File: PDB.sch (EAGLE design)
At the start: 53 parts, among them J1 B06B-HCMKK, J2 B06B-HCMKK, J3 SS-6488-NF-A431, J4 SS-6488-NF-A431, J5 B06B-HCMKK, J6 B03B-HCMKS, J7 B03B-HCMKS, J8 SS-6488-NF-A431

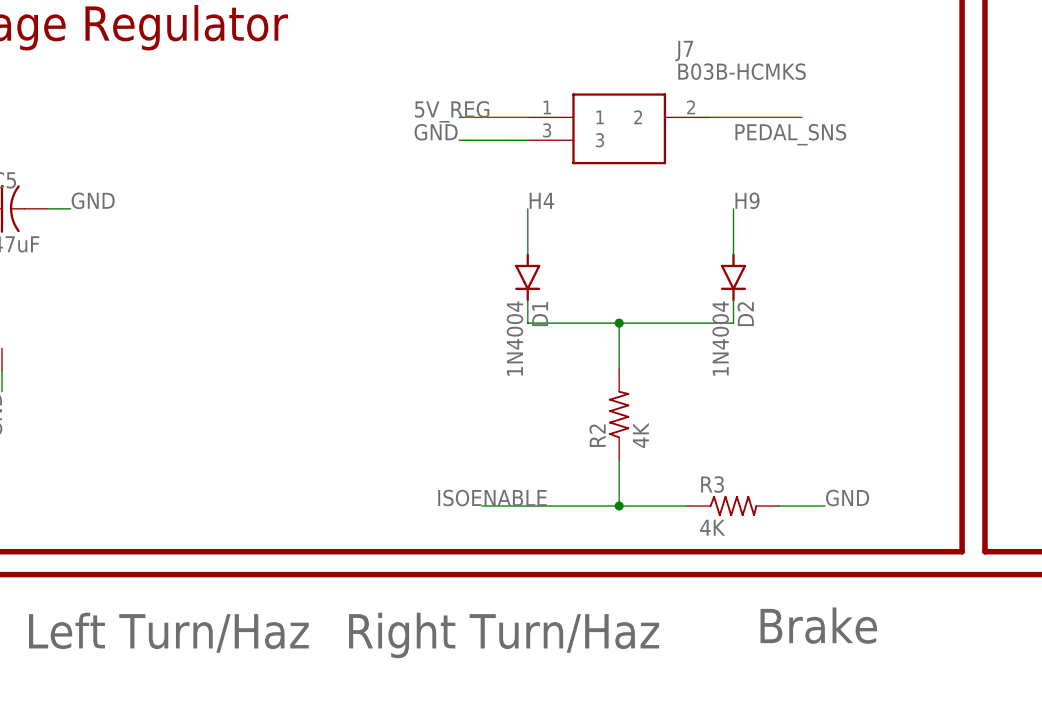
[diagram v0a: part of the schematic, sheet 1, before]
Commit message: Flipped all connectors to the back side, added capacitors connecting Teensy's 5V_REG to GND
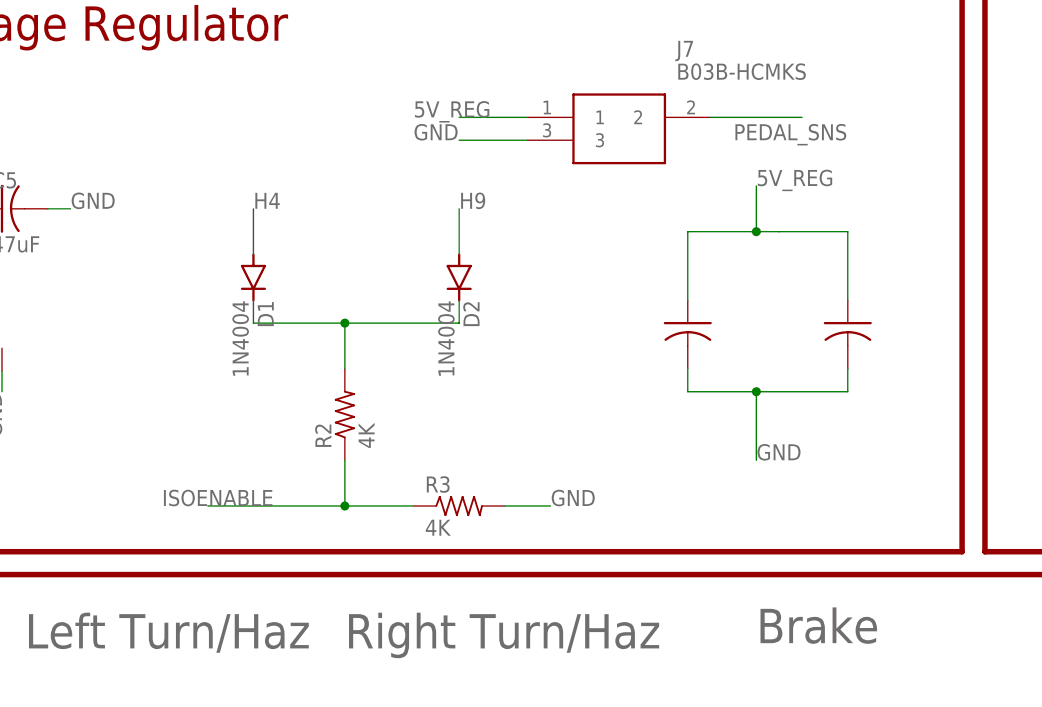
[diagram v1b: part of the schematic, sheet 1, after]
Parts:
- added C1: 0.1uF, rcl:C-USC0805
- added C2: 10uF, rcl:C-USC0805
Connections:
- net 5V_REG: now also C1.1, C2.1
- net GND: now also C1.2, C2.2
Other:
- moved on the sheet: D1, D2, R2, R3
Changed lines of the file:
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@@
 <part name="R2" library="master_library" deviceset="R-US_" device="R0805" package3d_urn="urn:adsk.eagle:package:2274104/1" value="4K"/>
 <part name="R3" library="master_library" deviceset="R-US_" device="R0805" package3d_urn="urn:adsk.eagle:package:2274104/1" value="4K"/>
+<part name="C1" library="rcl" library_urn="urn:adsk.eagle:library:334" deviceset="C-US" device="C0805" package3d_urn="urn:adsk.eagle:package:23617/2" value="0.1uF"/>
+<part name="C2" library="rcl" library_urn="urn:adsk.eagle:library:334" deviceset="C-US" device="C0805" package3d_urn="urn:adsk.eagle:package:23617/2" value="10uF"/>
 </parts>
 <sheets>
@@
 <attribute name="VALUE" x="223.012" y="119.888" size="1.778" layer="96" align="center-left"/>
 </instance>
-<instance part="D1" gate="1" x="-25.4" y="111.76" smashed="yes" rot="R270">
-<attribute name="NAME" x="-24.9174" y="109.22" size="1.778" layer="95" rot="R270"/>
-<attribute name="VALUE" x="-27.7114" y="109.22" size="1.778" layer="96" rot="R270"/>
-</instance>
-<instance part="D2" gate="1" x="-2.54" y="111.76" smashed="yes" rot="R270">
-<attribute name="NAME" x="-2.0574" y="109.22" size="1.778" layer="95" rot="R270"/>
-<attribute name="VALUE" x="-4.8514" y="109.22" size="1.778" layer="96" rot="R270"/>
-</instance>
-<instance part="R2" gate="G$1" x="-15.24" y="96.52" smashed="yes" rot="R90">
-<attribute name="NAME" x="-16.7386" y="92.71" size="1.778" layer="95" rot="R90"/>
-<attribute name="VALUE" x="-11.938" y="92.71" size="1.778" layer="96" rot="R90"/>
-</instance>
-<instance part="R3" gate="G$1" x="-2.54" y="86.36" smashed="yes">
-<attribute name="NAME" x="-6.35" y="87.8586" size="1.778" layer="95"/>
-<attribute name="VALUE" x="-6.35" y="83.058" size="1.778" layer="96"/>
-</instance>
+<instance part="D1" gate="1" x="-55.88" y="111.76" smashed="yes" rot="R270">
+<attribute name="NAME" x="-55.3974" y="109.22" size="1.778" layer="95" rot="R270"/>
+<attribute name="VALUE" x="-58.1914" y="109.22" size="1.778" layer="96" rot="R270"/>
+</instance>
+<instance part="D2" gate="1" x="-33.02" y="111.76" smashed="yes" rot="R270">
+<attribute name="NAME" x="-32.5374" y="109.22" size="1.778" layer="95" rot="R270"/>
+<attribute name="VALUE" x="-35.3314" y="109.22" size="1.778" layer="96" rot="R270"/>
+</instance>
+<instance part="R2" gate="G$1" x="-45.72" y="96.52" smashed="yes" rot="R90">
+<attribute name="NAME" x="-47.2186" y="92.71" size="1.778" layer="95" rot="R90"/>
+<attribute name="VALUE" x="-42.418" y="92.71" size="1.778" layer="96" rot="R90"/>
+</instance>
+<instance part="R3" gate="G$1" x="-33.02" y="86.36" smashed="yes">
+<attribute name="NAME" x="-36.83" y="87.8586" size="1.778" layer="95"/>
+<attribute name="VALUE" x="-36.83" y="83.058" size="1.778" layer="96"/>
+</instance>
+<instance part="C1" gate="G$1" x="10.16" y="106.68" smashed="yes"/>
+<instance part="C2" gate="G$1" x="-7.62" y="106.68" smashed="yes"/>
 </instances>
 <busses>
@@
 <segment>
 <pinref part="D1" gate="1" pin="A"/>
-<wire x1="-25.4" y1="114.3" x2="-25.4" y2="119.38" width="0.1524" layer="91"/>
-<label x="-25.4" y="119.38" size="1.778" layer="95"/>
+<wire x1="-55.88" y1="114.3" x2="-55.88" y2="119.38" width="0.1524" layer="91"/>
+<label x="-55.88" y="119.38" size="1.778" layer="95"/>
 </segment>
 </net>
@@
 <label x="-38.1" y="129.54" size="1.778" layer="95"/>
 </segment>
+<segment>
+<pinref part="C1" gate="G$1" pin="1"/>
+<wire x1="10.16" y1="109.22" x2="10.16" y2="116.84" width="0.1524" layer="91"/>
+<wire x1="10.16" y1="116.84" x2="2.54" y2="116.84" width="0.1524" layer="91"/>
+<pinref part="C2" gate="G$1" pin="1"/>
+<wire x1="0" y1="116.84" x2="-7.62" y2="116.84" width="0.1524" layer="91"/>
+<wire x1="-7.62" y1="109.22" x2="-7.62" y2="116.84" width="0.1524" layer="91"/>
+<wire x1="2.54" y1="116.84" x2="0" y2="116.84" width="0.1524" layer="91"/>
+<wire x1="0" y1="116.84" x2="0" y2="121.92" width="0.1524" layer="91"/>
+<junction x="0" y="116.84"/>
+<label x="0" y="121.92" size="1.778" layer="95"/>
+</segment>
 </net>
 <net name="10V_REG" class="0">
@@
 <segment>
 <pinref part="R3" gate="G$1" pin="2"/>
-<wire x1="2.54" y1="86.36" x2="7.62" y2="86.36" width="0.1524" layer="91"/>
-<label x="7.62" y="86.36" size="1.778" layer="95"/>
+<wire x1="-27.94" y1="86.36" x2="-22.86" y2="86.36" width="0.1524" layer="91"/>
+<label x="-22.86" y="86.36" size="1.778" layer="95"/>
+</segment>
+<segment>
+<pinref part="C1" gate="G$1" pin="2"/>
+<wire x1="10.16" y1="101.6" x2="10.16" y2="99.06" width="0.1524" layer="91"/>
+<wire x1="10.16" y1="99.06" x2="0" y2="99.06" width="0.1524" layer="91"/>
+<pinref part="C2" gate="G$1" pin="2"/>
+<wire x1="0" y1="99.06" x2="-7.62" y2="99.06" width="0.1524" layer="91"/>
+<wire x1="-7.62" y1="99.06" x2="-7.62" y2="101.6" width="0.1524" layer="91"/>
+<wire x1="0" y1="99.06" x2="0" y2="91.44" width="0.1524" layer="91"/>
+<junction x="0" y="99.06"/>
+<label x="0" y="91.44" size="1.778" layer="95"/>
 </segment>
 </net>
@@
 <segment>
 <pinref part="R2" gate="G$1" pin="1"/>
-<wire x1="-15.24" y1="91.44" x2="-15.24" y2="86.36" width="0.1524" layer="91"/>
-<wire x1="-15.24" y1="86.36" x2="-7.62" y2="86.36" width="0.1524" layer="91"/>
+<wire x1="-45.72" y1="91.44" x2="-45.72" y2="86.36" width="0.1524" layer="91"/>
+<wire x1="-45.72" y1="86.36" x2="-38.1" y2="86.36" width="0.1524" layer="91"/>
 <pinref part="R3" gate="G$1" pin="1"/>
-<wire x1="-15.24" y1="86.36" x2="-30.48" y2="86.36" width="0.1524" layer="91"/>
-<junction x="-15.24" y="86.36"/>
-<label x="-35.56" y="86.36" size="1.778" layer="95"/>
+<wire x1="-45.72" y1="86.36" x2="-60.96" y2="86.36" width="0.1524" layer="91"/>
+<junction x="-45.72" y="86.36"/>
+<label x="-66.04" y="86.36" size="1.778" layer="95"/>
 </segment>
 </net>
@@
 <segment>
 <pinref part="D2" gate="1" pin="A"/>
-<wire x1="-2.54" y1="114.3" x2="-2.54" y2="119.38" width="0.1524" layer="91"/>
-<label x="-2.54" y="119.38" size="1.778" layer="95"/>
+<wire x1="-33.02" y1="114.3" x2="-33.02" y2="119.38" width="0.1524" layer="91"/>
+<label x="-33.02" y="119.38" size="1.778" layer="95"/>
 </segment>
 </net>
@@
 <segment>
 <pinref part="D2" gate="1" pin="C"/>
-<wire x1="-2.54" y1="109.22" x2="-2.54" y2="106.68" width="0.1524" layer="91"/>
+<wire x1="-33.02" y1="109.22" x2="-33.02" y2="106.68" width="0.1524" layer="91"/>
 <pinref part="D1" gate="1" pin="C"/>
-<wire x1="-25.4" y1="109.22" x2="-25.4" y2="106.68" width="0.1524" layer="91"/>
-<wire x1="-2.54" y1="106.68" x2="-15.24" y2="106.68" width="0.1524" layer="91"/>
-<wire x1="-15.24" y1="106.68" x2="-25.4" y2="106.68" width="0.1524" layer="91"/>
-<wire x1="-15.24" y1="106.68" x2="-15.24" y2="101.6" width="0.1524" layer="91"/>
-<junction x="-15.24" y="106.68"/>
+<wire x1="-55.88" y1="109.22" x2="-55.88" y2="106.68" width="0.1524" layer="91"/>
+<wire x1="-33.02" y1="106.68" x2="-45.72" y2="106.68" width="0.1524" layer="91"/>
+<wire x1="-45.72" y1="106.68" x2="-55.88" y2="106.68" width="0.1524" layer="91"/>
+<wire x1="-45.72" y1="106.68" x2="-45.72" y2="101.6" width="0.1524" layer="91"/>
+<junction x="-45.72" y="106.68"/>
 <pinref part="R2" gate="G$1" pin="2"/>
 </segment>

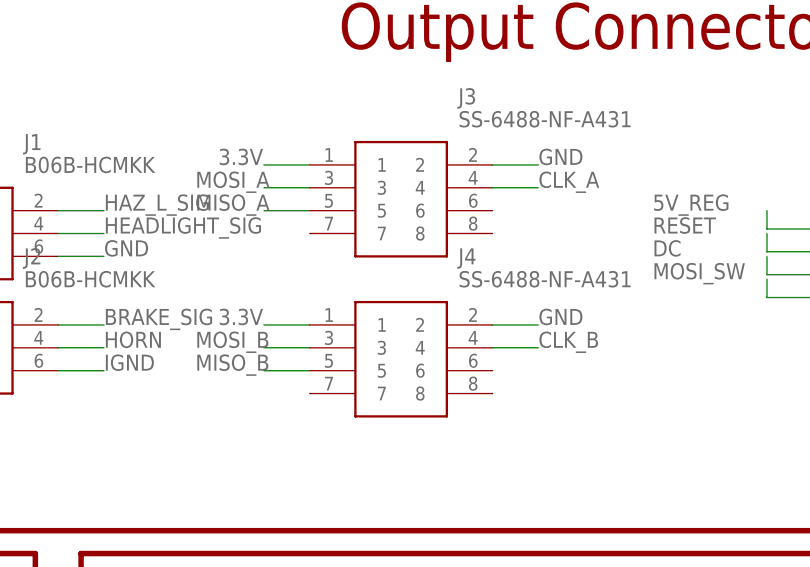
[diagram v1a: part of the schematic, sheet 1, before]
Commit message: Adjusted schematic and routing to pass twisted pairs to each signal
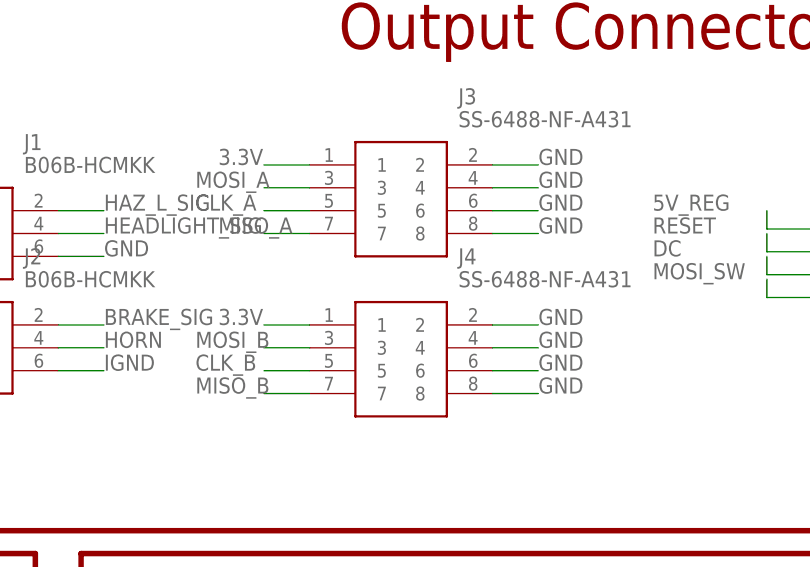
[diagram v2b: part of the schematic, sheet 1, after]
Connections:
- net CLK_A: now also J3.5; no longer J3.4
- net CLK_B: now also J4.5; no longer J4.4
- net GND: now also J3.4, J3.6, J3.8, J4.4, J4.6, J4.8
- net MISO_A: now also J3.7; no longer J3.5
- net MISO_B: now also J4.7; no longer J4.5
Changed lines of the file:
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@@
 <label x="0" y="91.44" size="1.778" layer="95"/>
+</segment>
+<segment>
+<pinref part="J3" gate="G$1" pin="4"/>
+<wire x1="170.18" y1="119.38" x2="175.26" y2="119.38" width="0.1524" layer="91"/>
+<label x="175.26" y="119.38" size="1.778" layer="95"/>
+</segment>
+<segment>
+<pinref part="J3" gate="G$1" pin="6"/>
+<wire x1="170.18" y1="116.84" x2="175.26" y2="116.84" width="0.1524" layer="91"/>
+<label x="175.26" y="116.84" size="1.778" layer="95"/>
+</segment>
+<segment>
+<pinref part="J3" gate="G$1" pin="8"/>
+<wire x1="170.18" y1="114.3" x2="175.26" y2="114.3" width="0.1524" layer="91"/>
+<label x="175.26" y="114.3" size="1.778" layer="95"/>
+</segment>
+<segment>
+<pinref part="J4" gate="G$1" pin="4"/>
+<wire x1="170.18" y1="101.6" x2="175.26" y2="101.6" width="0.1524" layer="91"/>
+<label x="175.26" y="101.6" size="1.778" layer="95"/>
+</segment>
+<segment>
+<pinref part="J4" gate="G$1" pin="6"/>
+<wire x1="170.18" y1="99.06" x2="175.26" y2="99.06" width="0.1524" layer="91"/>
+<label x="175.26" y="99.06" size="1.778" layer="95"/>
+</segment>
+<segment>
+<pinref part="J4" gate="G$1" pin="8"/>
+<wire x1="170.18" y1="96.52" x2="175.26" y2="96.52" width="0.1524" layer="91"/>
+<label x="175.26" y="96.52" size="1.778" layer="95"/>
 </segment>
 </net>
@@
 <net name="CLK_A" class="0">
 <segment>
-<pinref part="J3" gate="G$1" pin="4"/>
-<wire x1="170.18" y1="119.38" x2="175.26" y2="119.38" width="0.1524" layer="91"/>
-<label x="175.26" y="119.38" size="1.778" layer="95"/>
-</segment>
-<segment>
 <pinref part="U$3" gate="G$1" pin="D32/A13/SCK1/TX4"/>
 <wire x1="147.32" y1="-15.24" x2="142.24" y2="-15.24" width="0.1524" layer="91"/>
 <label x="139.7" y="-15.24" size="1.778" layer="95"/>
 </segment>
-</net>
-<net name="MISO_A" class="0">
 <segment>
 <pinref part="J3" gate="G$1" pin="5"/>
@@
 <label x="137.16" y="116.84" size="1.778" layer="95"/>
 </segment>
+</net>
+<net name="MISO_A" class="0">
 <segment>
 <pinref part="U$3" gate="G$1" pin="D1/TOUCH/MISO1/TX1"/>
@@
 <label x="134.62" y="43.18" size="1.778" layer="95"/>
 </segment>
+<segment>
+<pinref part="J3" gate="G$1" pin="7"/>
+<wire x1="149.86" y1="114.3" x2="144.78" y2="114.3" width="0.1524" layer="91"/>
+<label x="139.7" y="114.3" size="1.778" layer="95"/>
+</segment>
 </net>
 <net name="MOSI_B" class="0">
@@
 <net name="MISO_B" class="0">
 <segment>
+<pinref part="U$3" gate="G$1" pin="D12/MISO0"/>
+<wire x1="147.32" y1="15.24" x2="142.24" y2="15.24" width="0.1524" layer="91"/>
+<label x="137.16" y="15.24" size="1.778" layer="95"/>
+</segment>
+<segment>
+<pinref part="J4" gate="G$1" pin="7"/>
+<wire x1="149.86" y1="96.52" x2="144.78" y2="96.52" width="0.1524" layer="91"/>
+<label x="137.16" y="96.52" size="1.778" layer="95"/>
+</segment>
+</net>
+<net name="CLK_B" class="0">
+<segment>
+<pinref part="U$3" gate="G$1" pin="D13/LED/SCK0"/>
+<wire x1="218.44" y1="15.24" x2="226.06" y2="15.24" width="0.1524" layer="91"/>
+<label x="226.06" y="15.24" size="1.778" layer="95"/>
+</segment>
+<segment>
 <pinref part="J4" gate="G$1" pin="5"/>
 <wire x1="149.86" y1="99.06" x2="144.78" y2="99.06" width="0.1524" layer="91"/>
 <label x="137.16" y="99.06" size="1.778" layer="95"/>
 </segment>
-<segment>
-<pinref part="U$3" gate="G$1" pin="D12/MISO0"/>
-<wire x1="147.32" y1="15.24" x2="142.24" y2="15.24" width="0.1524" layer="91"/>
-<label x="137.16" y="15.24" size="1.778" layer="95"/>
-</segment>
-</net>
-<net name="CLK_B" class="0">
-<segment>
-<pinref part="J4" gate="G$1" pin="4"/>
-<wire x1="170.18" y1="101.6" x2="175.26" y2="101.6" width="0.1524" layer="91"/>
-<label x="175.26" y="101.6" size="1.778" layer="95"/>
-</segment>
-<segment>
-<pinref part="U$3" gate="G$1" pin="D13/LED/SCK0"/>
-<wire x1="218.44" y1="15.24" x2="226.06" y2="15.24" width="0.1524" layer="91"/>
-<label x="226.06" y="15.24" size="1.778" layer="95"/>
-</segment>
-</net>
+</net>

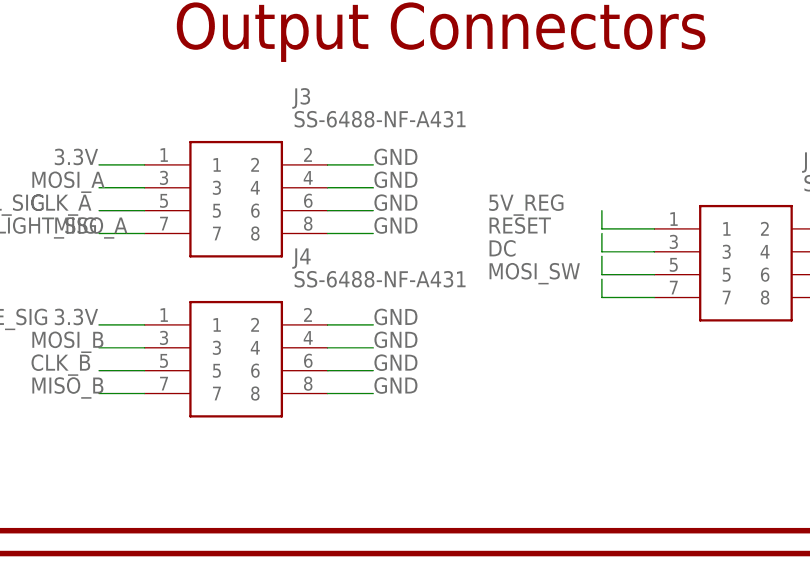
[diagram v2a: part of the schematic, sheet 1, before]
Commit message: adds cs signal but does not route it
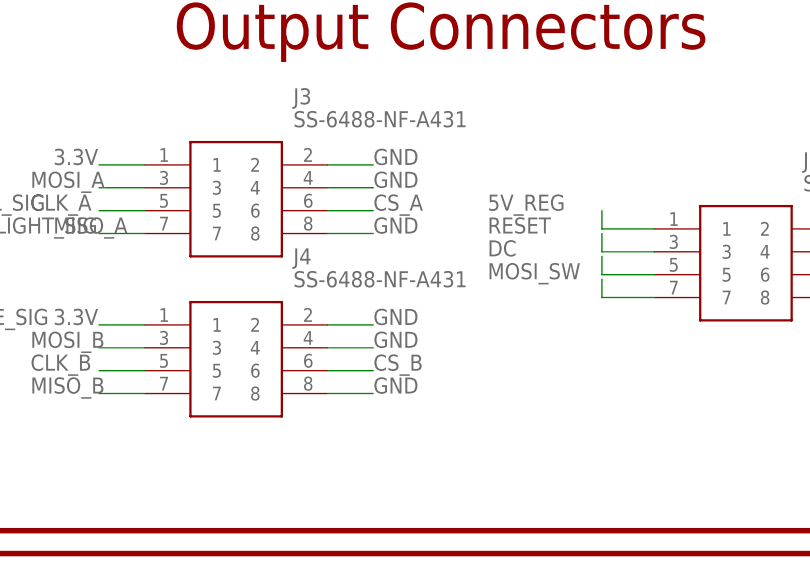
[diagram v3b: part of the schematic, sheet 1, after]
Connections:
- new net CS_A: J3.6
- new net CS_B: J4.6
- net GND: no longer J3.6, J4.6
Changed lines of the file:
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@@
-</segment>
-<segment>
-<pinref part="J3" gate="G$1" pin="6"/>
-<wire x1="170.18" y1="116.84" x2="175.26" y2="116.84" width="0.1524" layer="91"/>
-<label x="175.26" y="116.84" size="1.778" layer="95"/>
 </segment>
 <segment>
@@
 <wire x1="170.18" y1="101.6" x2="175.26" y2="101.6" width="0.1524" layer="91"/>
 <label x="175.26" y="101.6" size="1.778" layer="95"/>
-</segment>
-<segment>
-<pinref part="J4" gate="G$1" pin="6"/>
-<wire x1="170.18" y1="99.06" x2="175.26" y2="99.06" width="0.1524" layer="91"/>
-<label x="175.26" y="99.06" size="1.778" layer="95"/>
 </segment>
 <segment>
@@
 </segment>
 </net>
+<net name="CS_A" class="0">
+<segment>
+<pinref part="J3" gate="G$1" pin="6"/>
+<wire x1="170.18" y1="116.84" x2="175.26" y2="116.84" width="0.1524" layer="91"/>
+<label x="175.26" y="116.84" size="1.778" layer="95"/>
+</segment>
+</net>
+<net name="CS_B" class="0">
+<segment>
+<pinref part="J4" gate="G$1" pin="6"/>
+<wire x1="170.18" y1="99.06" x2="175.26" y2="99.06" width="0.1524" layer="91"/>
+<label x="175.26" y="99.06" size="1.778" layer="95"/>
+</segment>
+</net>
